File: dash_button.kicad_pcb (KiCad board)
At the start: 2 copper layers, 200 x 28 mm, 67 parts, among them J1 MINI 5PTP, J2 1050570001, J3 Debug, J4 JST PH 1x2, J5 JST PH 1x5, P1 CONN_02X03, Q1 AO3401A, Q11 AO3400A, Q12 AO3400A, Q13 AO3400A, Q14 AO3400A, Q15 AO3400A, Q2 AO3401A, Q3 AO3401A, Q4 AO3401A, Q6 AO3401A, Q7 AO3400A, SW1 TS-1002S-08526C, SW2 TS-1002S-08526C, SW3 TS-1002S-08526C, SW4 TS-1002S-08526C, SW5 TS-1002S-08526C, U1 ATtiny441-MUR, U2 HT7550-1

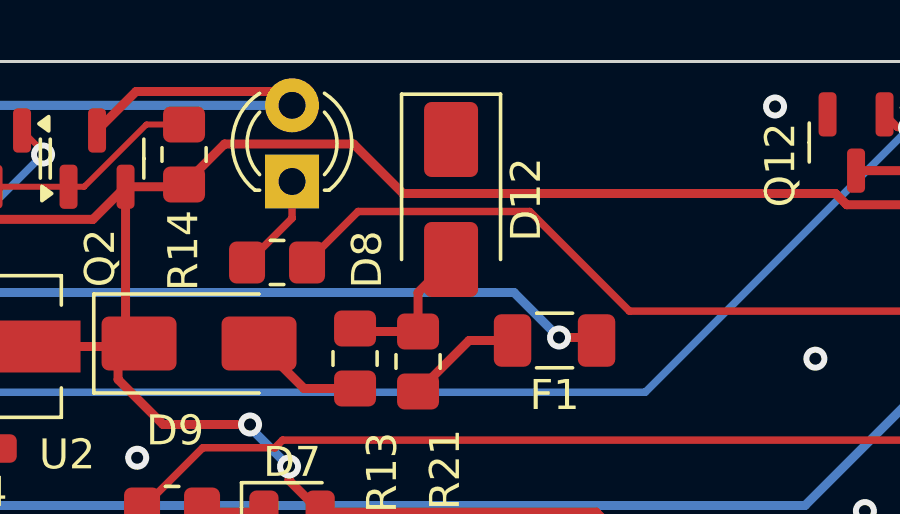
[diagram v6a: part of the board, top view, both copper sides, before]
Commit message: flip around TVS Diode
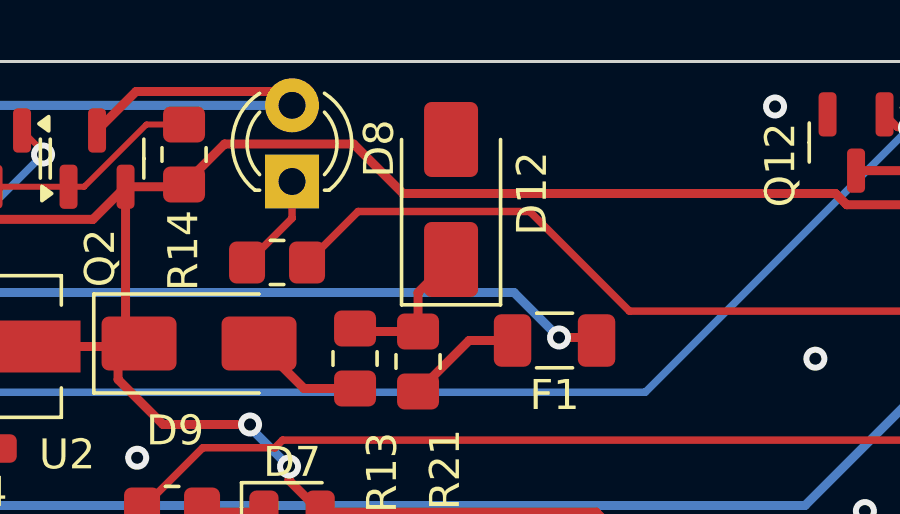
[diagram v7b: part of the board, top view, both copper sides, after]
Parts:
- turned D12 to 90 degrees
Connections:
- D12 pad 1: GND -> Net-(D12-A1)
- D12 pad 2: Net-(D12-A2) -> GND
- R13 pad 1: Net-(D12-A2) -> Net-(D12-A1)
- R21 pad 2: Net-(D12-A2) -> Net-(D12-A1)
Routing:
- net Net-(D12-A2): track 5.00 -> 0.00 mm
- net Net-(D12-A1): track 0.00 -> 5.00 mm
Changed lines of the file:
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@@
 	(net 51 "Net-(Q14-D)")
 	(net 52 "Net-(Q11-D)")
-	(net 53 "Net-(D12-A2)")
+	(net 53 "Net-(D12-A1)")
 	(net 54 "Net-(F1-Pad2)")
 	(net 55 "Net-(D9-A)")
@@
 	(footprint "Diode_SMD:D_SMA"
 		(layer "F.Cu")
-		(at 197.1 51.6 -90)
+		(at 197.1 51.6 90)
 		(descr "Diode SMA (DO-214AC)")
 		(tags "Diode SMA (DO-214AC)")
 		(property "Reference" "D12"
-			(at 0 -2.5 90)
+			(at 0.2 2.7 90)
 			(layer "F.SilkS")
 			(effects
@@
 		)
 		(property "Footprint" "Diode_SMD:D_SMA"
-			(at 0 0 -90)
+			(at 0 0 90)
 			(unlocked yes)
 			(layer "F.Fab")
@@
 		)
 		(property "Datasheet" "https://www.littelfuse.com/media?resourcetype=datasheets&itemid=75e32973-b177-4ee3-a0ff-cedaf1abdb93&filename=smaj-datasheet"
-			(at 0 0 -90)
+			(at 0 0 90)
 			(unlocked yes)
 			(layer "F.Fab")
@@
 		)
 		(property "Description" "400W unidirectional Transient Voltage Suppressor, 16.0Vr, SMA(DO-214AC)"
-			(at 0 0 -90)
+			(at 0 0 90)
 			(unlocked yes)
 			(layer "F.Fab")
@@
 		)
 		(property "Sim.Library" "Models/tvs_diod_smajxxx_a_spice_model.lib"
-			(at 0 0 -90)
+			(at 0 0 90)
 			(unlocked yes)
 			(layer "F.Fab")
@@
 		)
 		(property "Sim.Name" "SMAJ16A"
-			(at 0 0 -90)
+			(at 0 0 90)
 			(unlocked yes)
 			(layer "F.Fab")
@@
 		)
 		(property "Sim.Device" "SUBCKT"
-			(at 0 0 -90)
+			(at 0 0 90)
 			(unlocked yes)
 			(layer "F.Fab")
@@
 		)
 		(property "Sim.Pins" "1=1 2=2"
-			(at 0 0 -90)
+			(at 0 0 90)
 			(unlocked yes)
 			(layer "F.Fab")
@@
 		)
 		(property "LCSC Part #" "C908770"
-			(at 0 0 -90)
+			(at 0 0 90)
 			(unlocked yes)
 			(layer "F.Fab")
@@
 		)
 		(property "MPN" "SMAJ16A"
-			(at 0 0 -90)
+			(at 0 0 90)
 			(unlocked yes)
 			(layer "F.Fab")
@@
 		)
 		(property "Manufacturer" "GOODWORK"
-			(at 0 0 -90)
+			(at 0 0 90)
 			(unlocked yes)
 			(layer "F.Fab")
@@
 		(attr smd)
 		(fp_line
-			(start -3.51 1.65)
-			(end 2 1.65)
+			(start -3.51 -1.65)
+			(end 2 -1.65)
 			(stroke
 				(width 0.12)
@@
 		)
 		(fp_line
-			(start -3.51 -1.65)
-			(end 2 -1.65)
+			(start -3.51 1.65)
+			(end 2 1.65)
 			(stroke
 				(width 0.12)
@@
 		)
 		(fp_line
-			(start -3.5 1.75)
-			(end -3.5 -1.75)
+			(start 3.5 -1.75)
+			(end 3.5 1.75)
 			(stroke
 				(width 0.05)
@@
 		)
 		(fp_line
-			(start 3.5 1.75)
-			(end -3.5 1.75)
+			(start -3.5 -1.75)
+			(end 3.5 -1.75)
 			(stroke
 				(width 0.05)
@@
 		)
 		(fp_line
-			(start -3.5 -1.75)
-			(end 3.5 -1.75)
+			(start 3.5 1.75)
+			(end -3.5 1.75)
 			(stroke
 				(width 0.05)
@@
 		)
 		(fp_line
-			(start 3.5 -1.75)
-			(end 3.5 1.75)
+			(start -3.5 1.75)
+			(end -3.5 -1.75)
 			(stroke
 				(width 0.05)
@@
 		)
 		(fp_line
-			(start -2.3 1.5)
+			(start 2.3 -1.5)
 			(end -2.3 -1.5)
 			(stroke
@@
 		)
 		(fp_line
-			(start 2.3 1.5)
-			(end -2.3 1.5)
+			(start 2.3 -1.5)
+			(end 2.3 1.5)
 			(stroke
 				(width 0.1)
@@
 		)
 		(fp_line
-			(start 0.50118 0.75032)
-			(end 0.50118 -0.79908)
+			(start -0.64944 -0.79908)
+			(end -0.64944 0.80112)
 			(stroke
 				(width 0.1)
@@
 		)
 		(fp_line
-			(start -0.64944 0.00102)
-			(end 0.50118 0.75032)
+			(start 0.50118 0.00102)
+			(end 1.4994 0.00102)
 			(stroke
 				(width 0.1)
@@
 		(fp_line
 			(start -0.64944 0.00102)
-			(end -1.55114 0.00102)
+			(end 0.50118 -0.79908)
 			(stroke
 				(width 0.1)
@@
 		(fp_line
 			(start -0.64944 0.00102)
-			(end 0.50118 -0.79908)
+			(end -1.55114 0.00102)
 			(stroke
 				(width 0.1)
@@
 		)
 		(fp_line
-			(start 0.50118 0.00102)
-			(end 1.4994 0.00102)
+			(start -0.64944 0.00102)
+			(end 0.50118 0.75032)
 			(stroke
 				(width 0.1)
@@
 		)
 		(fp_line
-			(start -0.64944 -0.79908)
-			(end -0.64944 0.80112)
+			(start 0.50118 0.75032)
+			(end 0.50118 -0.79908)
 			(stroke
 				(width 0.1)
@@
 		)
 		(fp_line
-			(start 2.3 -1.5)
-			(end 2.3 1.5)
+			(start 2.3 1.5)
+			(end -2.3 1.5)
 			(stroke
 				(width 0.1)
@@
 		)
 		(fp_line
-			(start 2.3 -1.5)
+			(start -2.3 1.5)
 			(end -2.3 -1.5)
 			(stroke
@@
 		)
 		(pad "1" smd roundrect
-			(at -2 0 270)
+			(at -2 0 90)
 			(size 2.5 1.8)
 			(layers "F.Cu" "F.Paste" "F.Mask")
 			(roundrect_rratio 0.1388888889)
-			(net 1 "GND")
+			(net 53 "Net-(D12-A1)")
 			(pinfunction "A1")
 			(pintype "passive")
 		)
 		(pad "2" smd roundrect
-			(at 2 0 270)
+			(at 2 0 90)
 			(size 2.5 1.8)
 			(layers "F.Cu" "F.Paste" "F.Mask")
 			(roundrect_rratio 0.1388888889)
-			(net 53 "Net-(D12-A2)")
+			(net 1 "GND")
 			(pinfunction "A2")
 			(pintype "passive")
@@
 			(layers "F.Cu" "F.Paste" "F.Mask")
 			(roundrect_rratio 0.208333)
-			(net 53 "Net-(D12-A2)")
+			(net 53 "Net-(D12-A1)")
 			(pintype "passive")
 		)
@@
 		(tags "LED diameter 3.0mm 2 pins")
 		(property "Reference" "D8"
-			(at -2.6 2.5 -90)
+			(at 1.1 2.9 -90)
 			(layer "F.SilkS")
 			(effects
@@
 			(layers "F.Cu" "F.Paste" "F.Mask")
 			(roundrect_rratio 0.208333)
-			(net 53 "Net-(D12-A2)")
+			(net 53 "Net-(D12-A1)")
 			(pintype "passive")
 		)

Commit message: tag revision 4
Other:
- board text added: "Revision:rev4"
- board text removed: "Revision:rev3"
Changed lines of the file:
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@@
 		(layer "Edge.Cuts")
 	)
-	(gr_text "Revision:rev3"
+	(gr_text "Revision:rev4"
 		(at 63 72 0)
 		(layer "F.SilkS")
